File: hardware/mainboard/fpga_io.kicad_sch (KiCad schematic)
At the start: 25 parts

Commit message: Misc bits
Signed-off-by: David Shah <dave@ds0.me>
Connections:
- net B2BL_CLKO+: now also U?.Y12 (PB58A/+/PCLKT3_1/ADC_CP6/HS/BDQ60); no longer U?.W13 (PB60A/+/ADC_CP9/HS/BDQS60)
- net B2BL_CLKO-: now also U?.W12 (PB58B/-/PCLKC3_1/ADC_CN6/HS/BDQ60); no longer U?.U12 (PB62A/+/ADC_CP10/HS/BDQ60)
- net B2BL_DI1+: now also U?.W13 (PB60A/+/ADC_CP9/HS/BDQS60); no longer U?.Y12 (PB58A/+/PCLKT3_1/ADC_CP6/HS/BDQ60)
- net B2BL_DI1-: now also U?.U12 (PB62A/+/ADC_CP10/HS/BDQ60); no longer U?.W12 (PB58B/-/PCLKC3_1/ADC_CN6/HS/BDQ60)
- net B2BL_DO0+: now also U?.R12 (PB64A/+/ADC_CP4/HS/BDQ60); no longer U?.V12 (PB60B/-/ADC_CN9/HS/BDQSN60)
- net B2BL_DO0-: now also U?.P12 (PB64B/-/ADC_CN4/HS/BDQ60); no longer U?.T12 (PB62B/-/ADC_CN10/HS/BDQ60)
- net B2BL_DO1+: now also U?.Y13 (PB66A/+/COMP1IP/HS/BDQ60); no longer U?.R12 (PB64A/+/ADC_CP4/HS/BDQ60)
- net B2BL_DO1-: now also U?.Y14 (PB66B/-/COMP1IN/HS/BDQ60); no longer U?.P12 (PB64B/-/ADC_CN4/HS/BDQ60)
- net B2BR_MISC2: now reaches U?.E2 (PL15A/+)
- net B2BR_MISC1: now reaches U?.E3 (PL13B/-)
- net B2BR_MISC0: now reaches U?.E4 (PL13A/+)
- net B2BL_MISC1: now reaches U?.E7 (PL11A/+)
- net B2BL_MISC2: now reaches U?.E8 (PL11B/-)
- net B2BL_MISC0: now reaches U?.E9 (PL10B/-)
- net B2BR_DI2+: now reaches U?.P13 (PB70A/+/COMP2IP/HS/BDQ76)
- net B2BR_DI2-: now reaches U?.R13 (PB70B/-/COMP2IN/HS/BDQ76)
- net B2BL_DO2-: now reaches U?.U14 (PB68B/-/ADC_CN8/HS/BDQ60)
- net B2BL_DO2+: now reaches U?.V14 (PB68A/+/ADC_CP8/HS/BDQ60)
- net B2BR_DO2+: now reaches U?.W18 (PB84A/+/LRC_GPLL0T_IN/HS/BDQ76)
- net B2BR_DO2-: now reaches U?.Y18 (PB84B/-/LRC_GPLL0C_IN/VREF3_2/HS/BDQ76)
- new net B2BL_DI2+: U?.V12 (PB60B/-/ADC_CN9/HS/BDQSN60)
- new net B2BL_DI2-: U?.T12 (PB62B/-/ADC_CN10/HS/BDQ60)

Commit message: More stuff
Signed-off-by: David Shah <dave@ds0.me>
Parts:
- added C? (x3): 470n, symbol Device:C_Small
- added C? (x2): 10µ, symbol Device:C_Small
- added X?: XO32, Oscillator:Oscillator_SMD_EuroQuartz_XO32-4Pin_3.2x2.5mm, symbol Oscillator:XO32
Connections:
- net +1V8: now also U?.N17 (VCCIO2), U?.U19 (VCCIO2), U?.V3 (VCCIO5), C?.1, C?.1, C?.1, C?.1
- net +3V3: now also C?.2, X?.4 (V+)
- net B2BL_MISC0: now also U?.U1 (PB4A/+/CDR_RXP0/VREF5_1/ADC_CP0/COMP1P/HS)
- net B2BL_MISC1: now also U?.T1 (PB4B/-/CDR_RXN0/ADC_CN0/COMP1N/HS)
- net B2BL_MISC2: now also U?.V1 (PB6A/+/PCLKT5_0/CDR_RXP1/ADC_CP1/COMP2P/HS)
- net B2BR_MISC0: now also U?.Y2 (PB8A/+/PCLKT5_1/LLC_GPLL0T_IN/ADC_CP3/HS)
- net B2BR_MISC1: now also U?.Y3 (PB8B/-/PCLKC5_1/LLC_GPLL0C_IN/ADC_CN3/HS)
- net B2BR_MISC2: now also U?.R5 (PB10A/+/PCLKT5_2/ADC_CP2/COMP3P/HS)
- net GND: now also C?.1, C?.2, C?.2, C?.2, C?.2, X?.2 (GND)
- net CLK48: now reaches U?.L13 (PR17A/+/PCLKT1_2)
- net CLK48: now also X?.3 (OUT)
- net M2_~RST: now reaches U?.M4 (PL36A/+)
- net M2_DISABLE2: now reaches U?.M5 (PL36B/-)
- net M2_DISABLE1: now reaches U?.M6 (PL38A/+)
- net EAR_0: now reaches U?.N6 (PL42A/+)
- net EAR_1: now reaches U?.N7 (PL42B/-)
- net EAR_2: now reaches U?.P1 (PL44A/+)
- net EAR_3: now reaches U?.P2 (PL44B/-)
- net CLK100+: no longer names the net of U?.R7 (PB18A/+/PCLKT4_3/HS/BDQ22)
- net CLK100-: no longer names the net of U?.T7 (PB18B/-/PCLKC4_3/HS/BDQ22)
- no-connect marks 0 -> 1

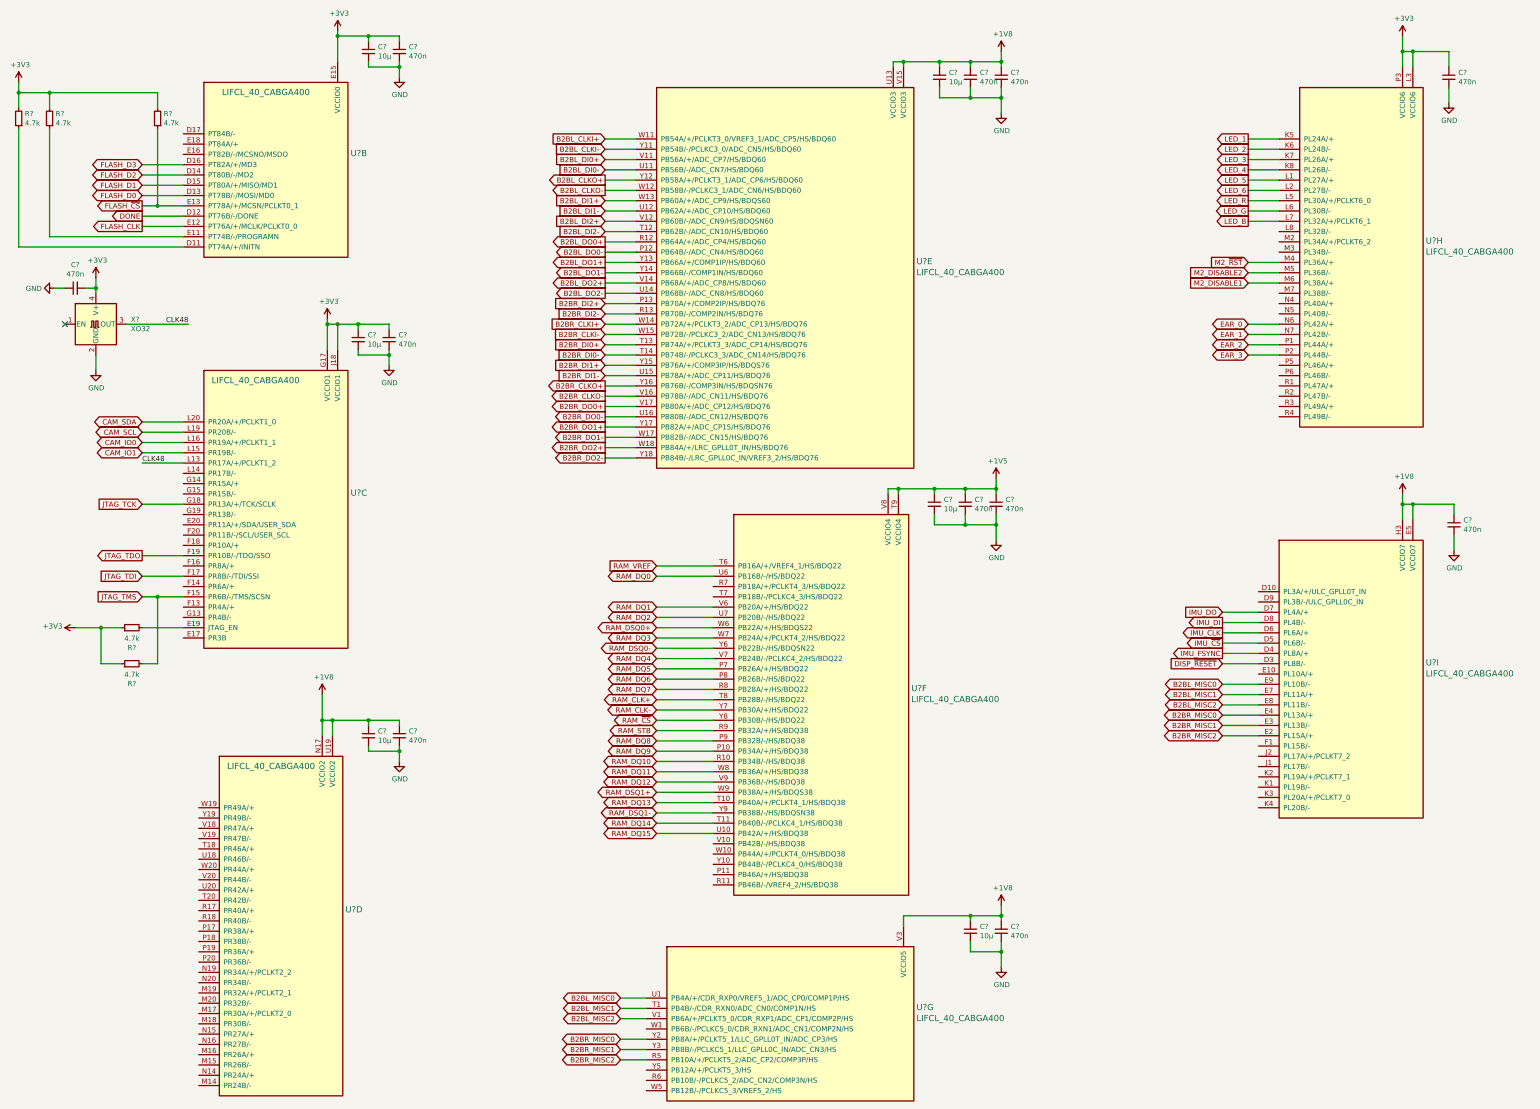
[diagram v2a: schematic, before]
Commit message: Annotate and assign some footpints
Signed-off-by: David Shah <dave@ds0.me>
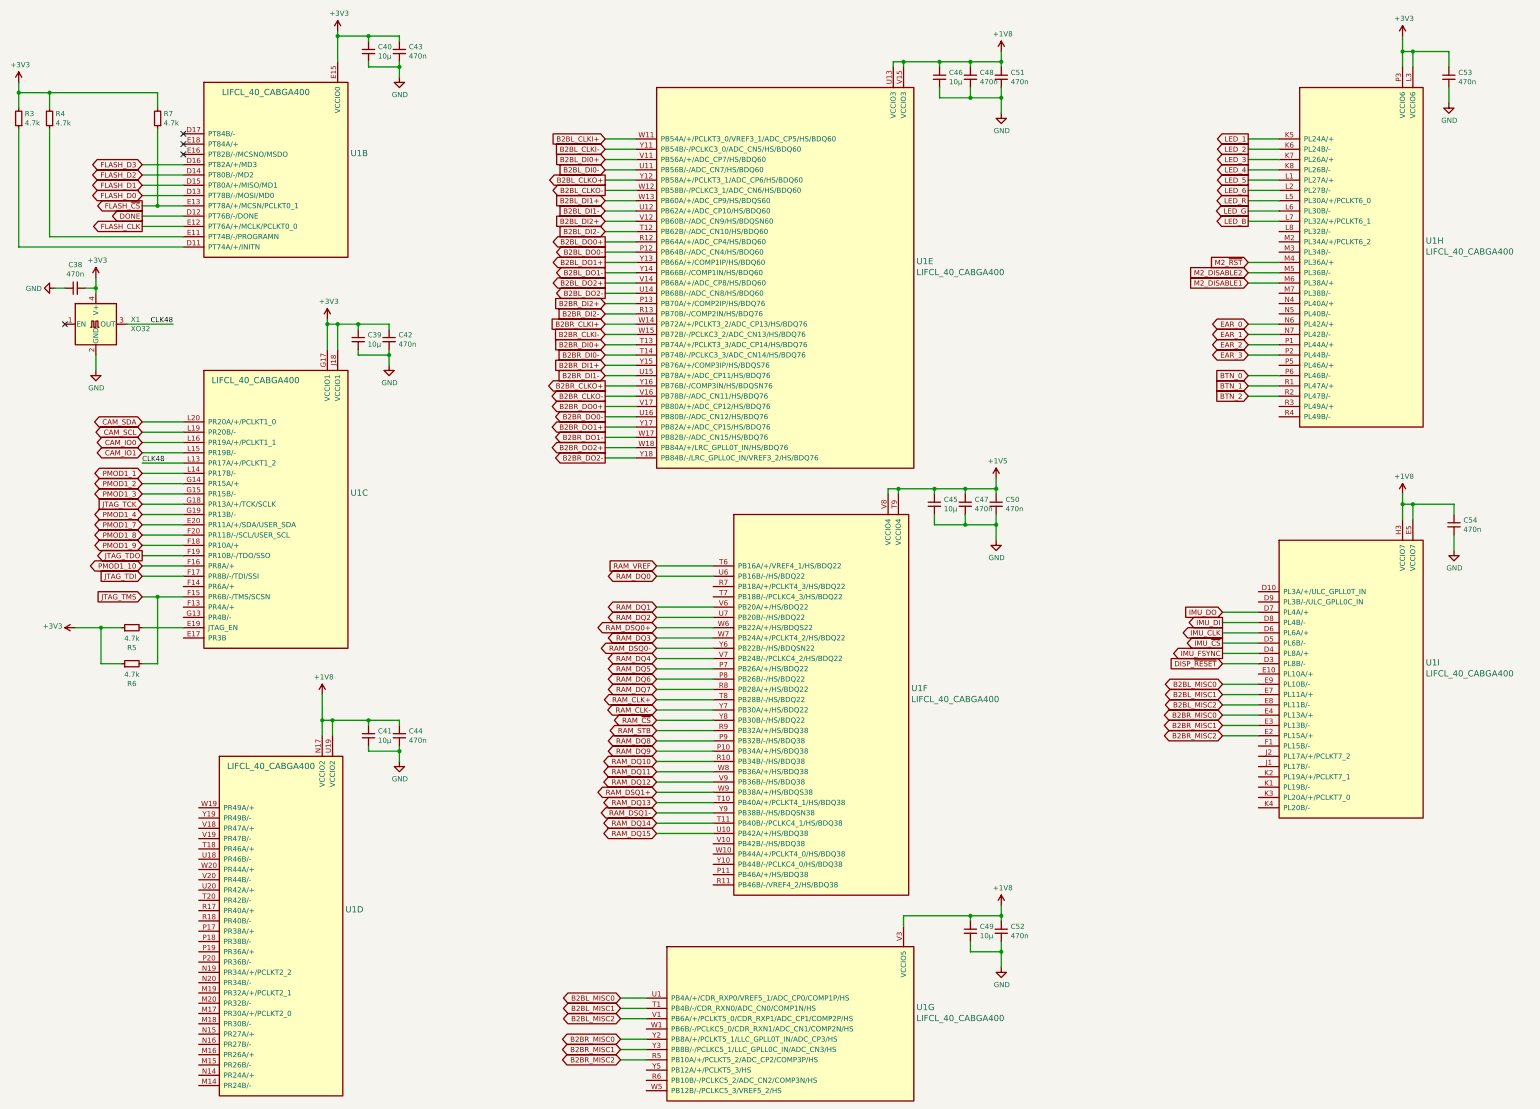
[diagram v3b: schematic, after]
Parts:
- C38, C42, C43, C44, C47, C48, C50, C51, C52, C53, C54: renamed from C?; footprint (none) -> Capacitor_SMD:C_0402_1005Metric
- C39, C40, C41, C45, C46, C49: renamed from C?; footprint (none) -> Capacitor_SMD:C_0805_2012Metric
- R3, R4, R5, R6, R7: renamed from R?; footprint (none) -> Resistor_SMD:R_0402_1005Metric
- gave numbers to parts that had none: 2
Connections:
- net PMOD1_7: now reaches U1.E20 (PR11A/+/SDA/USER_SDA)
- net PMOD1_10: now reaches U1.F16 (PR8A/+)
- net PMOD1_9: now reaches U1.F18 (PR10A/+)
- net PMOD1_8: now reaches U1.F20 (PR11B/-/SCL/USER_SCL)
- net PMOD1_2: now reaches U1.G14 (PR15A/+)
- net PMOD1_3: now reaches U1.G15 (PR15B/-)
- net PMOD1_4: now reaches U1.G19 (PR13B/-)
- net PMOD1_1: now reaches U1.L14 (PR17B/-)
- net BTN_0: now reaches U1.P6 (PL46B/-)
- net BTN_1: now reaches U1.R1 (PL47A/+)
- net BTN_2: now reaches U1.R2 (PL47B/-)
- no-connect marks 1 -> 4

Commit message: Add and assign more footprints
Signed-off-by: David Shah <dave@ds0.me>
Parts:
- U1: footprint (none) -> meowality:BGA-400_20x20_17.0x17.0mm
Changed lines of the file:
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@@
       (effects (font (size 1.524 1.524)) (justify left))
     )
-    (property "Footprint" "" (id 2) (at 64.77 43.18 0)
+    (property "Footprint" "meowality:BGA-400_20x20_17.0x17.0mm" (id 2) (at 64.77 43.18 0)
       (effects (font (size 1.524 1.524)) (justify right) hide)
     )
@@
       (effects (font (size 1.524 1.524)) (justify left))
     )
-    (property "Footprint" "" (id 2) (at 179.07 256.54 0)
+    (property "Footprint" "meowality:BGA-400_20x20_17.0x17.0mm" (id 2) (at 179.07 256.54 0)
       (effects (font (size 1.524 1.524)) (justify right) hide)
     )
@@
       (effects (font (size 1.524 1.524)) (justify left))
     )
-    (property "Footprint" "" (id 2) (at 64.77 114.3 0)
+    (property "Footprint" "meowality:BGA-400_20x20_17.0x17.0mm" (id 2) (at 64.77 114.3 0)
       (effects (font (size 1.524 1.524)) (justify right) hide)
     )
@@
       (effects (font (size 1.524 1.524)) (justify left))
     )
-    (property "Footprint" "" (id 2) (at 330.2 156.21 0)
+    (property "Footprint" "meowality:BGA-400_20x20_17.0x17.0mm" (id 2) (at 330.2 156.21 0)
       (effects (font (size 1.524 1.524)) (justify right) hide)
     )
@@
       (effects (font (size 1.524 1.524)) (justify left))
     )
-    (property "Footprint" "" (id 2) (at 68.58 209.55 0)
+    (property "Footprint" "meowality:BGA-400_20x20_17.0x17.0mm" (id 2) (at 68.58 209.55 0)
       (effects (font (size 1.524 1.524)) (justify right) hide)
     )
@@
       (effects (font (size 1.524 1.524)) (justify left))
     )
-    (property "Footprint" "" (id 2) (at 335.28 44.45 0)
+    (property "Footprint" "meowality:BGA-400_20x20_17.0x17.0mm" (id 2) (at 335.28 44.45 0)
       (effects (font (size 1.524 1.524)) (justify right) hide)
     )
@@
       (effects (font (size 1.524 1.524)) (justify left))
     )
-    (property "Footprint" "" (id 2) (at 195.58 149.86 0)
+    (property "Footprint" "meowality:BGA-400_20x20_17.0x17.0mm" (id 2) (at 195.58 149.86 0)
       (effects (font (size 1.524 1.524)) (justify right) hide)
     )
@@
       (effects (font (size 1.524 1.524)) (justify left))
     )
-    (property "Footprint" "" (id 2) (at 176.53 44.45 0)
-      (effects (font (size 1.524 1.524)) (justify right) hide)
-    )
+    (property "Footprint" "meowality:BGA-400_20x20_17.0x17.0mm" (id 2) (at 176.53 44.45 0)
+      (effects (font (size 1.524 1.524)) (justify right) hide)
+    )

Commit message: Working on layout
Signed-off-by: David Shah <dave@ds0.me>
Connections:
- net BTN_2: no longer names the net of U1.R2 (PL47B/-)
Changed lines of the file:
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@@
-    (stroke (width 0) (type solid) (color 0 0 0 0))
-  )
-  (wire (pts (xy 323.85 109.22) (xy 331.47 109.22))
     (stroke (width 0) (type solid) (color 0 0 0 0))
   )
@@
       (effects (font (size 1.27 1.27)) (justify right) hide)
     )
-  )
-  (global_label "BTN_2" (shape input) (at 323.85 109.22 180)
-    (effects (font (size 1.27 1.27)) (justify right))
-    (property "Intersheet References" "${INTERSHEET_REFS}" (id 0) (at 314.1677 109.1406 0)
-      (effects (font (size 1.27 1.27)) (justify right) hide)
-    )

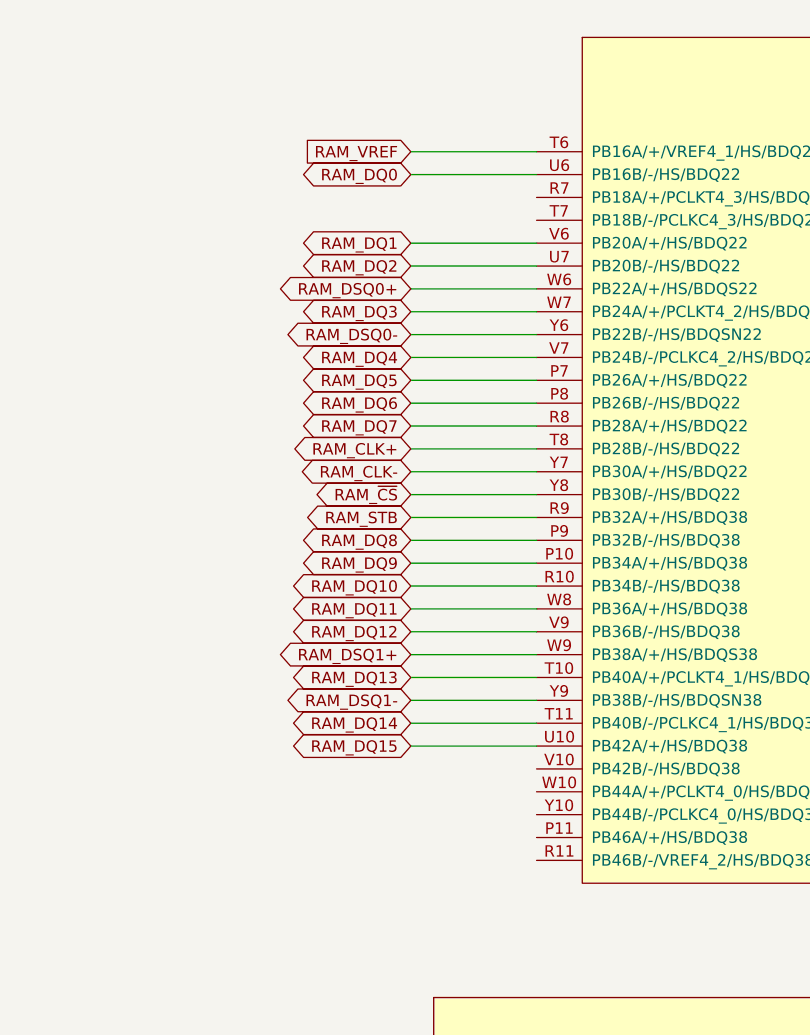
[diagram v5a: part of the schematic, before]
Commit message: DRAM routing
Signed-off-by: David Shah <dave@ds0.me>
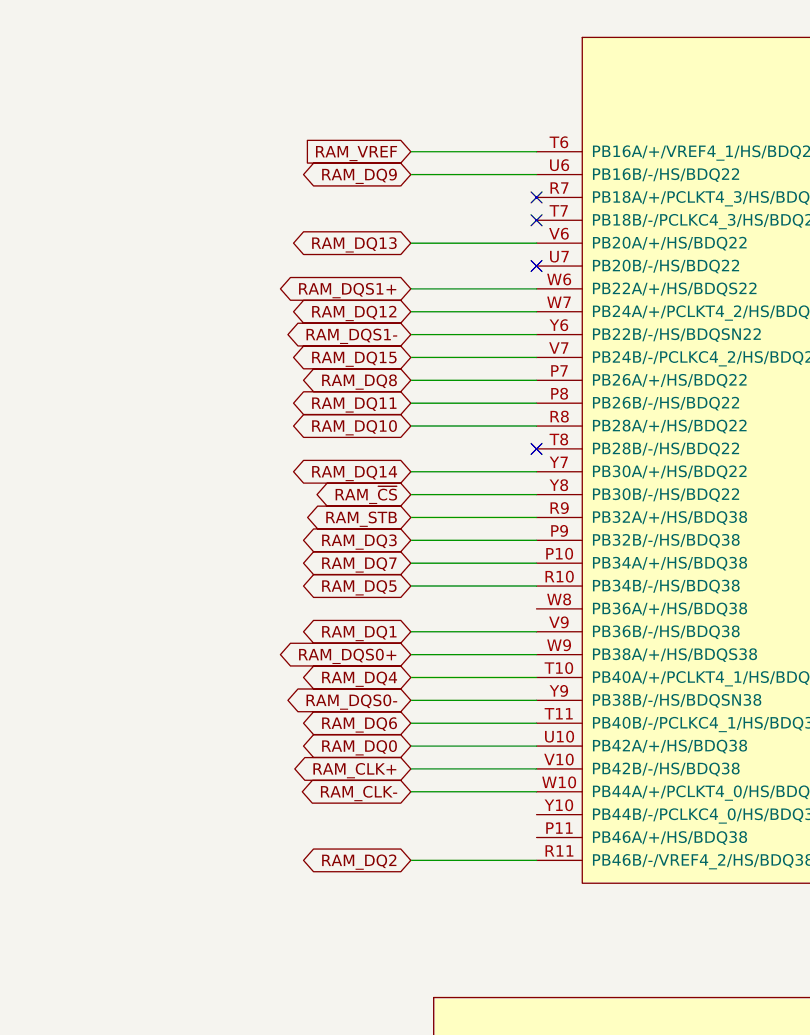
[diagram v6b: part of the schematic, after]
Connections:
- net RAM_CLK+: now also U1.V10 (PB42B/-/HS/BDQ38); no longer U1.T8 (PB28B/-/HS/BDQ22)
- net RAM_CLK-: now also U1.W10 (PB44A/+/PCLKT4_0/HS/BDQ38); no longer U1.Y7 (PB30A/+/HS/BDQ22)
- net RAM_DQ0: now also U1.U10 (PB42A/+/HS/BDQ38); no longer U1.U6 (PB16B/-/HS/BDQ22)
- net RAM_DQ1: now also U1.V9 (PB36B/-/HS/BDQ38); no longer U1.V6 (PB20A/+/HS/BDQ22)
- net RAM_DQ10: now also U1.R8 (PB28A/+/HS/BDQ22); no longer U1.R10 (PB34B/-/HS/BDQ38)
- net RAM_DQ11: now also U1.P8 (PB26B/-/HS/BDQ22); no longer U1.W8 (PB36A/+/HS/BDQ38)
- net RAM_DQ12: now also U1.W7 (PB24A/+/PCLKT4_2/HS/BDQ22); no longer U1.V9 (PB36B/-/HS/BDQ38)
- net RAM_DQ13: now also U1.V6 (PB20A/+/HS/BDQ22); no longer U1.T10 (PB40A/+/PCLKT4_1/HS/BDQ38)
- net RAM_DQ14: now also U1.Y7 (PB30A/+/HS/BDQ22); no longer U1.T11 (PB40B/-/PCLKC4_1/HS/BDQ38)
- net RAM_DQ15: now also U1.V7 (PB24B/-/PCLKC4_2/HS/BDQ22); no longer U1.U10 (PB42A/+/HS/BDQ38)
- net RAM_DQ2: now also U1.R11 (PB46B/-/VREF4_2/HS/BDQ38); no longer U1.U7 (PB20B/-/HS/BDQ22)
- net RAM_DQ3: now also U1.P9 (PB32B/-/HS/BDQ38); no longer U1.W7 (PB24A/+/PCLKT4_2/HS/BDQ22)
- net RAM_DQ4: now also U1.T10 (PB40A/+/PCLKT4_1/HS/BDQ38); no longer U1.V7 (PB24B/-/PCLKC4_2/HS/BDQ22)
- net RAM_DQ5: now also U1.R10 (PB34B/-/HS/BDQ38); no longer U1.P7 (PB26A/+/HS/BDQ22)
- net RAM_DQ6: now also U1.T11 (PB40B/-/PCLKC4_1/HS/BDQ38); no longer U1.P8 (PB26B/-/HS/BDQ22)
- net RAM_DQ7: now also U1.P10 (PB34A/+/HS/BDQ38); no longer U1.R8 (PB28A/+/HS/BDQ22)
- net RAM_DQ8: now also U1.P7 (PB26A/+/HS/BDQ22); no longer U1.P9 (PB32B/-/HS/BDQ38)
- net RAM_DQ9: now also U1.U6 (PB16B/-/HS/BDQ22); no longer U1.P10 (PB34A/+/HS/BDQ38)
- net RAM_DSQ0+ renamed RAM_DQS1+
- net RAM_DSQ0- renamed RAM_DQS1-
- net RAM_DSQ1+ renamed RAM_DQS0+
- net RAM_DSQ1- renamed RAM_DQS0-
- no-connect marks 4 -> 8
